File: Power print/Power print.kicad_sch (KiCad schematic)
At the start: 42 parts, among them IC1 INA3221AIRGVR, IC2 TPS566247DRLR, J1 USB_C_Receptacle_USB2.0_14P, J2 Microcontroller, J3 Vout_Connector, Q1 BC846, Q2 ZXMP4A16G, Q3 BC846, SW1 SW_Push, U1 CH224K

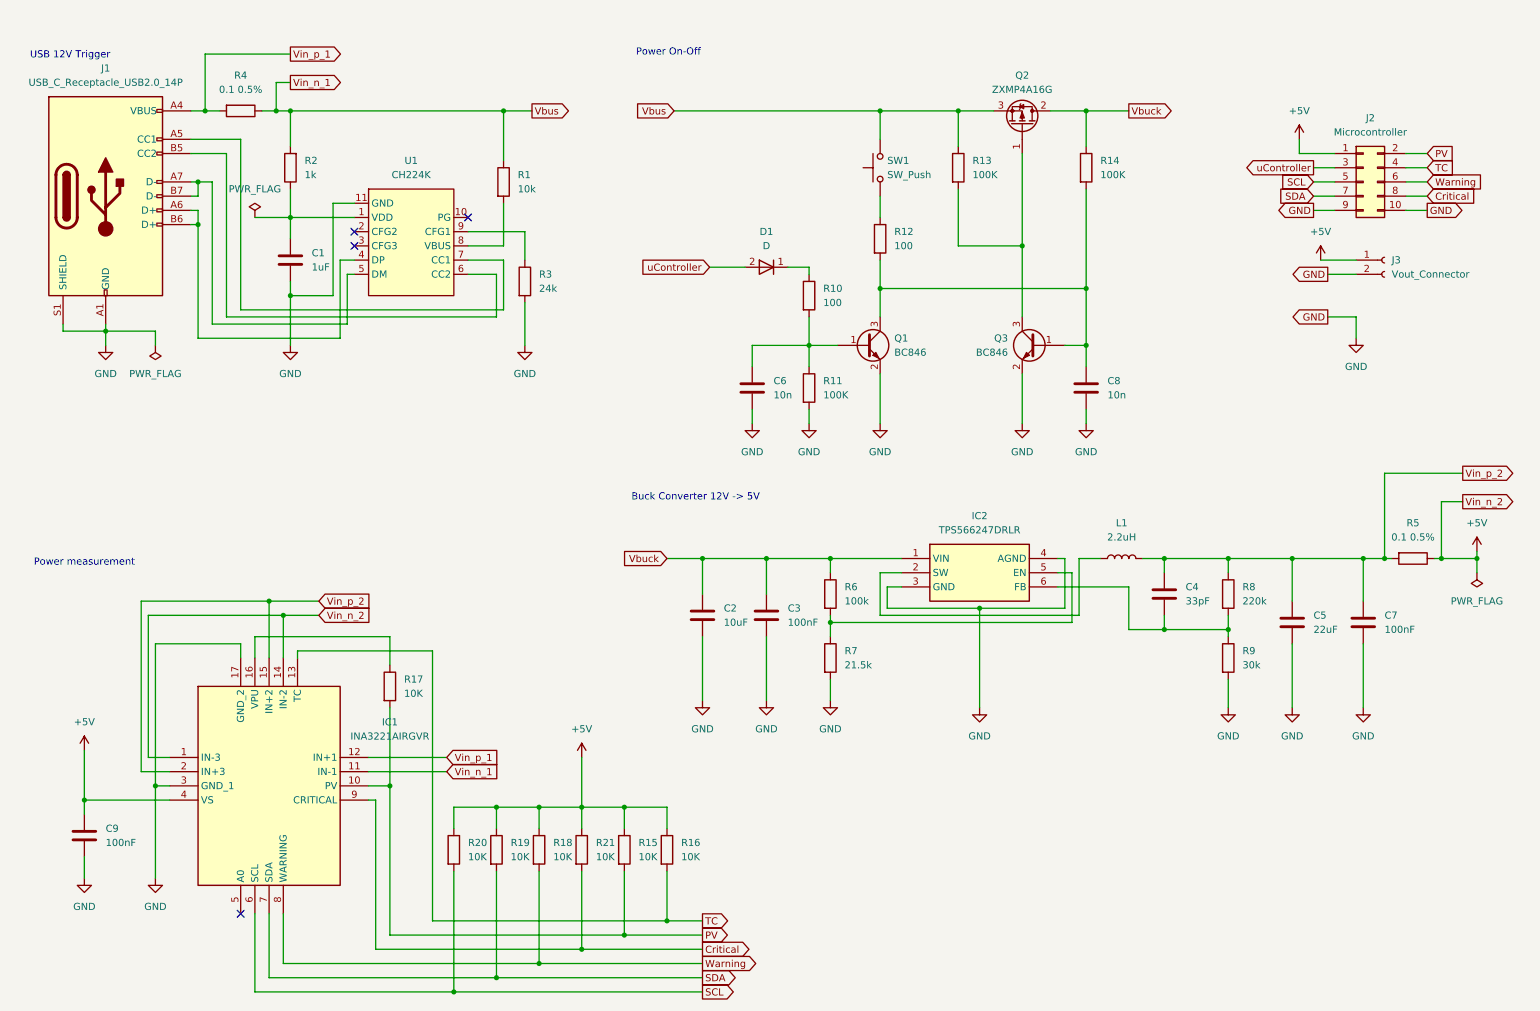
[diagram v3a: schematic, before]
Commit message: Power print schematics
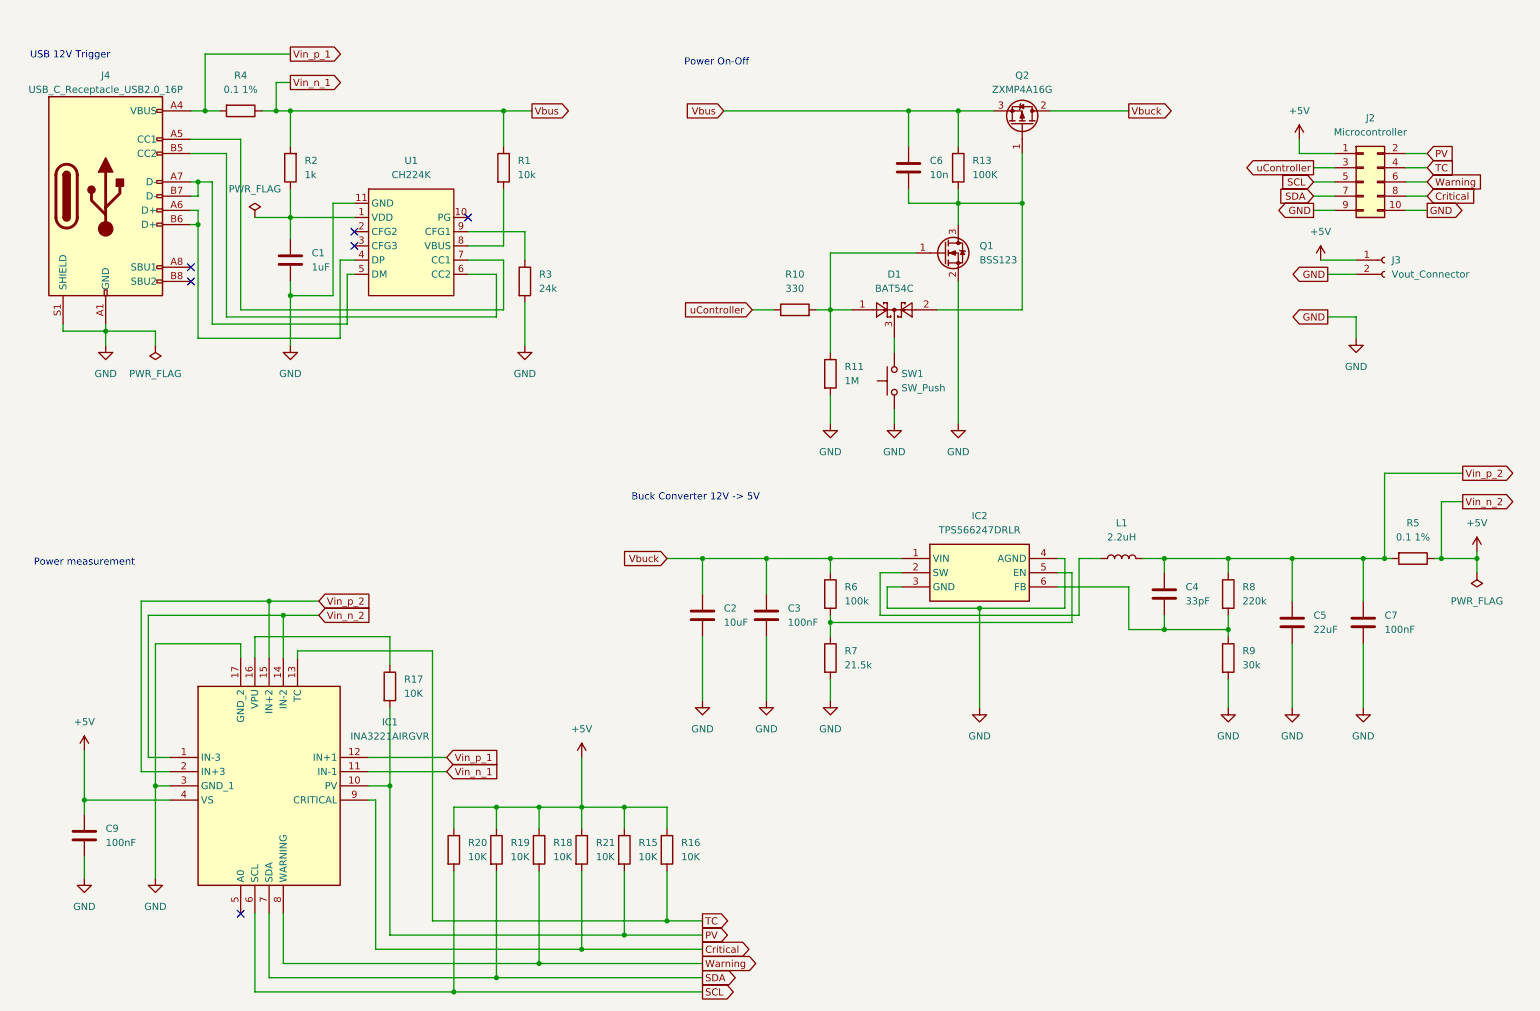
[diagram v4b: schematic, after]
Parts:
- removed C8: 10n, symbol Device:C
- removed D1: D, symbol Simulation_SPICE:D
- removed J1: USB_C_Receptacle_USB2.0_14P, symbol Connector:USB_C_Receptacle_USB2.0_14P
- removed Q1, Q3: BC846, Package_TO_SOT_SMD:SOT-23, symbol Transistor_BJT:BC846
- removed R12: 100, symbol Device:R
- removed R14: 100K, symbol Device:R
- added D1: BAT54C, Package_TO_SOT_SMD:SOT-23, symbol Diode:BAT54C
- added J4: USB_C_Receptacle_USB2.0_16P, Connector_USB:USB_C_Receptacle_GCT_USB4105-xx-A_16P_TopMnt_Horizontal, symbol Connector:USB_C_Receptacle_USB2.0_16P
- added Q1: BSS123, Package_TO_SOT_SMD:SOT-23, symbol Transistor_FET:BSS123
- C1: footprint (none) -> Capacitor_SMD:C_1206_3216Metric_Pad1.33x1.80mm_HandSolder; LCSC (none) -> C1848
- C2: footprint (none) -> Capacitor_SMD:C_1206_3216Metric_Pad1.33x1.80mm_HandSolder; LCSC (none) -> C1849
- C3, C7, C9: footprint (none) -> Capacitor_SMD:C_1206_3216Metric_Pad1.33x1.80mm_HandSolder; LCSC (none) -> C1945
- C4: footprint (none) -> Capacitor_SMD:C_1206_3216Metric_Pad1.33x1.80mm_HandSolder; LCSC (none) -> C1906
- C5: footprint (none) -> Capacitor_SMD:C_1206_3216Metric_Pad1.33x1.80mm_HandSolder; LCSC (none) -> C12891
- C6: footprint (none) -> Capacitor_SMD:C_0805_2012Metric_Pad1.18x1.45mm_HandSolder; LCSC (none) -> C1710
- IC1: footprint QFN65P400X400X100-17N-D -> PCBLIB_QFN-16_L4.0-W4.0-P0.65-TL-EP2.2_2024-11-15:QFN-16_L4.0-W4.0-P0.65-TL-EP2.2; LCSC (none) -> C181255
- IC2: footprint SOTFL50P160X60-6N -> PCBLIB_SOT-5X3-6_W1.6-L1.2-P0.50-LS1.6-BL_2024-11-15:SOT-5X3-6_W1.6-L1.2-P0.50-LS1.6-BL; LCSC (none) -> C5219274
- J2: footprint (none) -> Connector_PinHeader_2.54mm:PinHeader_2x05_P2.54mm_Vertical; LCSC (none) -> C7501276
- J3: footprint (none) -> PCBLIB_CONN-TH_P5.00_KF301-5.0-2P_2024-11-15:CONN-TH_P5.00_KF301-5.0-2P; LCSC (none) -> C474881
- L1: footprint (none) -> PCBLIB_IND-SMD_L7.2-W6.6_GPSR07X0_2024-11-15:IND-SMD_L7.2-W6.6_GPSR07X0; LCSC (none) -> C5189746
- Q2: LCSC (none) -> C141324
- R1, R15, R16, R17, R18, R19, R20, R21: footprint (none) -> Resistor_SMD:R_1206_3216Metric_Pad1.30x1.75mm_HandSolder; LCSC (none) -> C326700
- R10: value 100 -> 330; footprint (none) -> Resistor_SMD:R_1206_3216Metric_Pad1.30x1.75mm_HandSolder; LCSC (none) -> C3013376
- R11: value 100K -> 1M; footprint (none) -> Resistor_SMD:R_1210_3225Metric_Pad1.30x2.65mm_HandSolder; LCSC (none) -> C470029
- R13, R6: footprint (none) -> Resistor_SMD:R_1206_3216Metric_Pad1.30x1.75mm_HandSolder; LCSC (none) -> C606185
- R2: footprint Resistor_SMD:R_0805_2012Metric -> Resistor_SMD:R_1206_3216Metric_Pad1.30x1.75mm_HandSolder; LCSC (none) -> C2759097
- R3: footprint (none) -> Resistor_SMD:R_1206_3216Metric_Pad1.30x1.75mm_HandSolder; LCSC (none) -> C2759176
- R4, R5: value 0.1 0.5% -> 0.1 1%; footprint Resistor_SMD:R_2512_6332Metric -> Resistor_SMD:R_2512_6332Metric_Pad1.40x3.35mm_HandSolder; LCSC (none) -> C7419997
- R7: footprint (none) -> Resistor_SMD:R_1206_3216Metric_Pad1.30x1.75mm_HandSolder; LCSC (none) -> C311938
- R8: footprint (none) -> Resistor_SMD:R_1210_3225Metric_Pad1.30x2.65mm_HandSolder; LCSC (none) -> C606197
- R9: footprint (none) -> Resistor_SMD:R_1206_3216Metric_Pad1.30x1.75mm_HandSolder; LCSC (none) -> C3013378
- SW1: footprint Connector_PinHeader_1.27mm:PinHeader_1x02_P1.27mm_Vertical -> Connector_PinHeader_2.54mm:PinHeader_1x02_P2.54mm_Vertical; LCSC (none) -> C2685195
- U1: footprint tyk_common:ESSOP-10 -> PCBLIB_ESSOP-10_L4.9-W3.9-P1.0-LS6.0-TL-EP_2024-11-15:ESSOP-10_L4.9-W3.9-P1.0-LS6.0-TL-EP; LCSC (none) -> C970725
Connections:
- net GND: now also SW1.1, J4.A1 (GND), J4.A12 (GND), J4.B1 (GND), J4.B12 (GND), J4.S1 (SHIELD), Q1.2 (S); no longer C6.2
- net Vbus: now also C6.1; no longer SW1.2
- net Vin_p_1: now also J4.A4 (VBUS), J4.A9 (VBUS), J4.B4 (VBUS), J4.B9 (VBUS)
- net uController: now also R10.1
- net at R10.2, R11.1: now also D1.1, Q1.1 (G); no longer C6.1
- net at U1.4 (DP): now also J4.A6 (D+), J4.B6 (D+)
- net at U1.5 (DM): now also J4.A7 (D-), J4.B7 (D-)
- net at U1.6 (CC2): now also J4.B5 (CC2)
- net at U1.7 (CC1): now also J4.A5 (CC1)
- net at Q2.1 (G), R13.2: now also C6.2, D1.2, Q1.3 (D)
- new net: D1.3, SW1.2
- no-connect marks 4 -> 6
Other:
- moved on the sheet: R1, R10, R11

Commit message: PCB design
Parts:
- removed J2: Microcontroller, Connector_PinHeader_2.54mm:PinHeader_2x05_P2.54mm_Vertical, symbol Connector_Generic:Conn_02x05_Odd_Even
- removed R16: 10K, Resistor_SMD:R_1206_3216Metric_Pad1.30x1.75mm_HandSolder, symbol Device:R
- removed SW1: SW_Push, Connector_PinHeader_2.54mm:PinHeader_1x02_P2.54mm_Vertical, symbol Switch:SW_Push
- added J1: Conn_01x03_Pin, Connector_PinHeader_1.00mm:PinHeader_1x03_P1.00mm_Vertical, symbol Connector:Conn_01x03_Pin
- added J2: Conn_01x07_Pin, Connector_PinHeader_1.00mm:PinHeader_1x07_P1.00mm_Vertical, symbol Connector:Conn_01x07_Pin
- IC2: footprint PCBLIB_SOT-5X3-6_W1.6-L1.2-P0.50-LS1.6-BL_2024-11-15:SOT-5X3-6_W1.6-L1.2-P0.50-LS1.6-BL -> Package_TO_SOT_SMD:SOT-563
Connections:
- net +5V: now also J2.1 (Pin_1)
- net Critical: now also J2.5 (Pin_5)
- net GND: now also J1.2 (Pin_2), J2.7 (Pin_7)
- net PV: now also J2.6 (Pin_6)
- net SCL: now also J2.2 (Pin_2)
- net SDA: now also J2.3 (Pin_3)
- net Warning: now also J2.4 (Pin_4)
- net uController: now also J1.3 (Pin_3)
- net SW1: now reaches D1.3
- net SW1: now also J1.1 (Pin_1)
- net TC: no longer names the net of IC1.13 (TC)
- no-connect marks 6 -> 7
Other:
- company: (none) -> Cryptable
- title: (none) -> Pi Powermgmnt
- moved on the sheet: J3

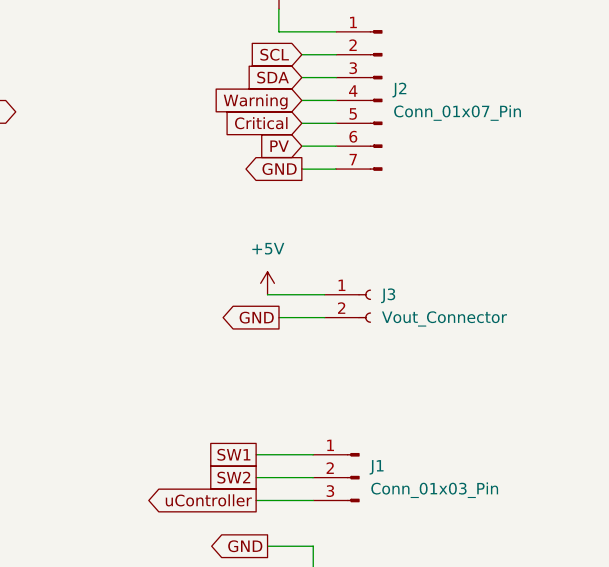
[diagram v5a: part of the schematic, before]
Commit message: Rotated power connector
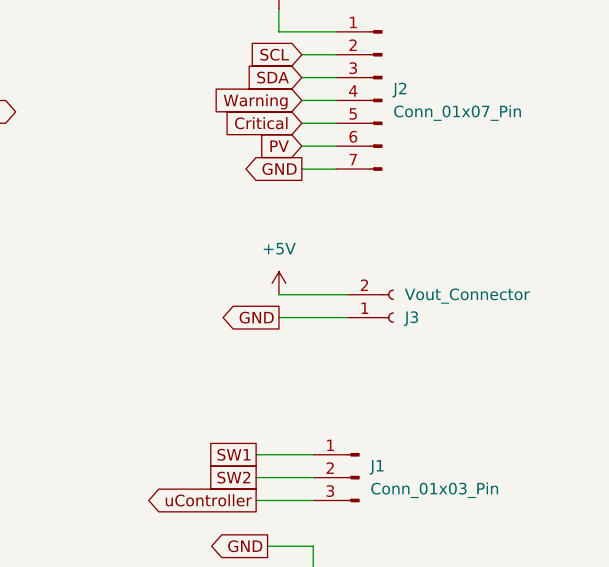
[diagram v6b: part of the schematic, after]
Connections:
- net +5V: now also J3.2 (Pin_2); no longer J3.1 (Pin_1)
- net GND: now also J3.1 (Pin_1); no longer J3.2 (Pin_2)
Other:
- moved on the sheet: J3
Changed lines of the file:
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@@
 	(wire
 		(pts
+			(xy 250.19 53.34) (xy 257.81 53.34)
+		)
+		(stroke
+			(width 0)
+			(type default)
+		)
+	)
+	(wire
+		(pts
 			(xy 41.91 146.05) (xy 38.1 146.05)
 		)
@@
 	(wire
 		(pts
-			(xy 250.19 53.34) (xy 255.27 53.34)
-		)
-		(stroke
-			(width 0)
-			(type default)
-		)
-	)
-	(wire
-		(pts
 			(xy 194.31 38.1) (xy 194.31 46.99)
 		)
@@
 	(wire
 		(pts
+			(xy 250.19 50.8) (xy 257.81 50.8)
+		)
+		(stroke
+			(width 0)
+			(type default)
+		)
+	)
+	(wire
+		(pts
 			(xy 39.37 125.73) (xy 54.61 125.73)
 		)
@@
 	(wire
 		(pts
-			(xy 248.92 50.8) (xy 255.27 50.8)
-		)
-		(stroke
-			(width 0)
-			(type default)
-		)
-	)
-	(wire
-		(pts
 			(xy 130.81 110.49) (xy 137.16 110.49)
 		)
@@
 	(symbol
 		(lib_id "power:+5V")
-		(at 248.92 50.8 0)
+		(at 250.19 50.8 0)
 		(unit 1)
 		(exclude_from_sim no)
@@
 		(fields_autoplaced yes)
 		(property "Reference" "#PWR017"
-			(at 248.92 54.61 0)
+			(at 250.19 54.61 0)
 			(effects
 				(font
@@
 		)
 		(property "Value" "+5V"
-			(at 248.92 45.72 0)
+			(at 250.19 45.72 0)
 			(effects
 				(font
@@
 		)
 		(property "Footprint" ""
-			(at 248.92 50.8 0)
+			(at 250.19 50.8 0)
 			(effects
 				(font
@@
 		)
 		(property "Datasheet" ""
-			(at 248.92 50.8 0)
+			(at 250.19 50.8 0)
 			(effects
 				(font
@@
 		)
 		(property "Description" "Power symbol creates a global label with name \"+5V\""
-			(at 248.92 50.8 0)
+			(at 250.19 50.8 0)
 			(effects
 				(font
@@
 	(symbol
 		(lib_id "Connector:Conn_01x02_Socket")
-		(at 260.35 50.8 0)
+		(at 262.89 53.34 0)
+		(mirror x)
 		(unit 1)
 		(exclude_from_sim no)
@@
 		(on_board yes)
 		(dnp no)
-		(fields_autoplaced yes)
 		(property "Reference" "J3"
-			(at 261.62 50.7999 0)
+			(at 264.16 53.3401 0)
 			(effects
 				(font
@@
 		)
 		(property "Value" "Vout_Connector"
-			(at 261.62 53.3399 0)
+			(at 264.16 50.8001 0)
 			(effects
 				(font
@@
 		)
 		(property "Footprint" "PCBLIB_CONN-TH_P5.00_KF301-5.0-2P_2024-11-15:CONN-TH_P5.00_KF301-5.0-2P"
-			(at 260.35 50.8 0)
+			(at 262.89 53.34 0)
 			(effects
 				(font
@@
 		)
 		(property "Datasheet" "~"
-			(at 260.35 50.8 0)
+			(at 262.89 53.34 0)
 			(effects
 				(font
@@
 		)
 		(property "Description" "Generic connector, single row, 01x02, script generated"
-			(at 260.35 50.8 0)
+			(at 262.89 53.34 0)
 			(effects
 				(font
@@
 		)
 		(property "Sim.Type" ""
-			(at 260.35 50.8 0)
+			(at 262.89 53.34 0)
 			(effects
 				(font
@@
 		)
 		(property "LCSC" "C474881"
-			(at 260.35 50.8 0)
+			(at 262.89 53.34 0)
 			(effects
 				(font
@@
 		)
 		(property "Sim.Params" ""
-			(at 260.35 50.8 0)
+			(at 262.89 53.34 0)
 			(effects
 				(font

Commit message: update schema
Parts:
- R5: value 0.1 1% -> 0.02 1%
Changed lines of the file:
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@@
 			)
 		)
-		(property "Value" "0.1 1%"
+		(property "Value" "0.02 1%"
 			(at 264.16 106.68 90)
 			(effects
